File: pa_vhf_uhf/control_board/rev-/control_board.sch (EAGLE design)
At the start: 0 parts

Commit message: minor updates to control board.
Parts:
- added ADC1: ADS1115, vtgs:ADS1115
- added J1: USB_B_PTH, SparkFun-Connectors:USB_B_PTH
- added U$1: SPX3819M5_5V, kj4qlp:V_REG_SPX3819-SOT23-5
- added U$2: ATMEGA32U4-AU, adafruit:ATMEGA32U4-AU
- added U$3: DECOTEC_102040-002B, vtgs:DECOTEC_102040-002B
- added X1: (no value), SparkFun-Retired:DB25_MALED

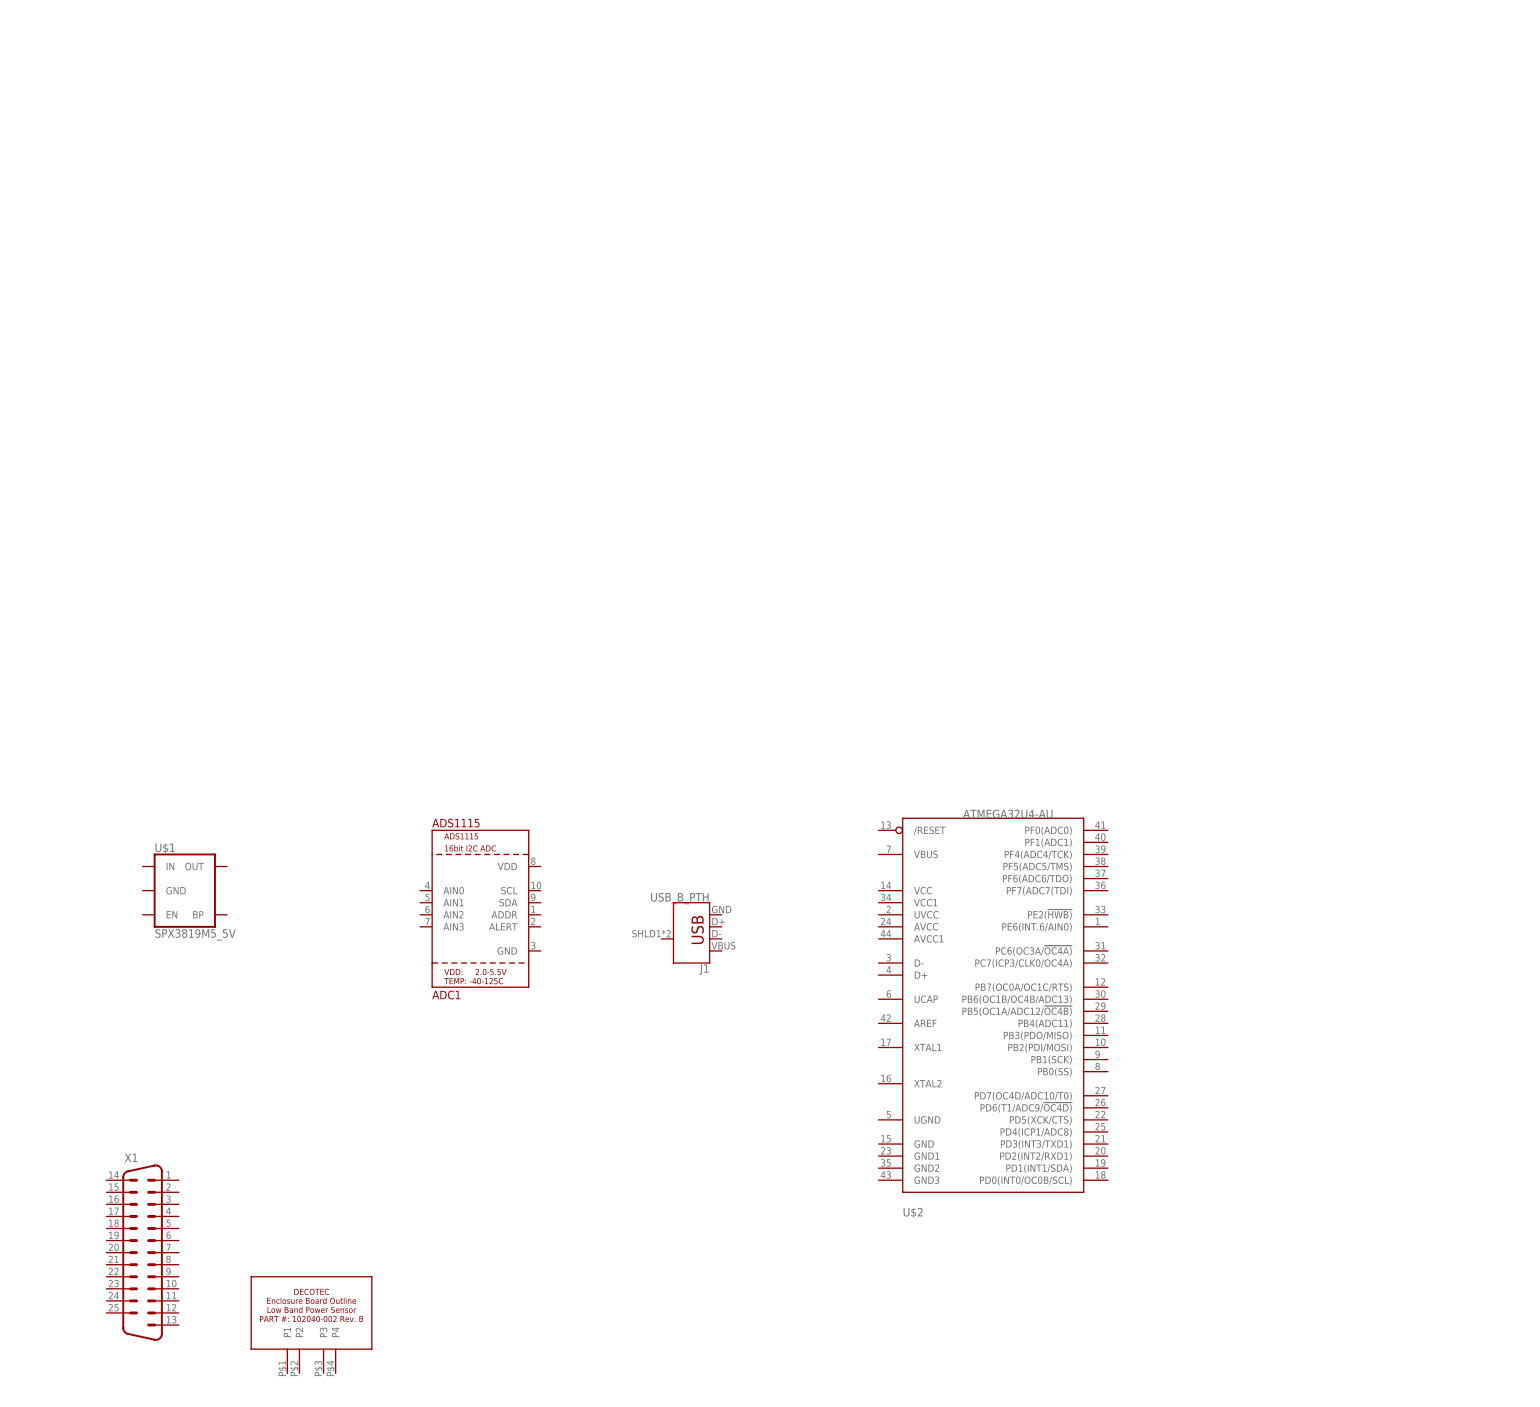
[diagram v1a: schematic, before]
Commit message: lots of updates, almost done, a bit more tweaking/refining of the layout.  need to double check optocoupler current levels/resistors.
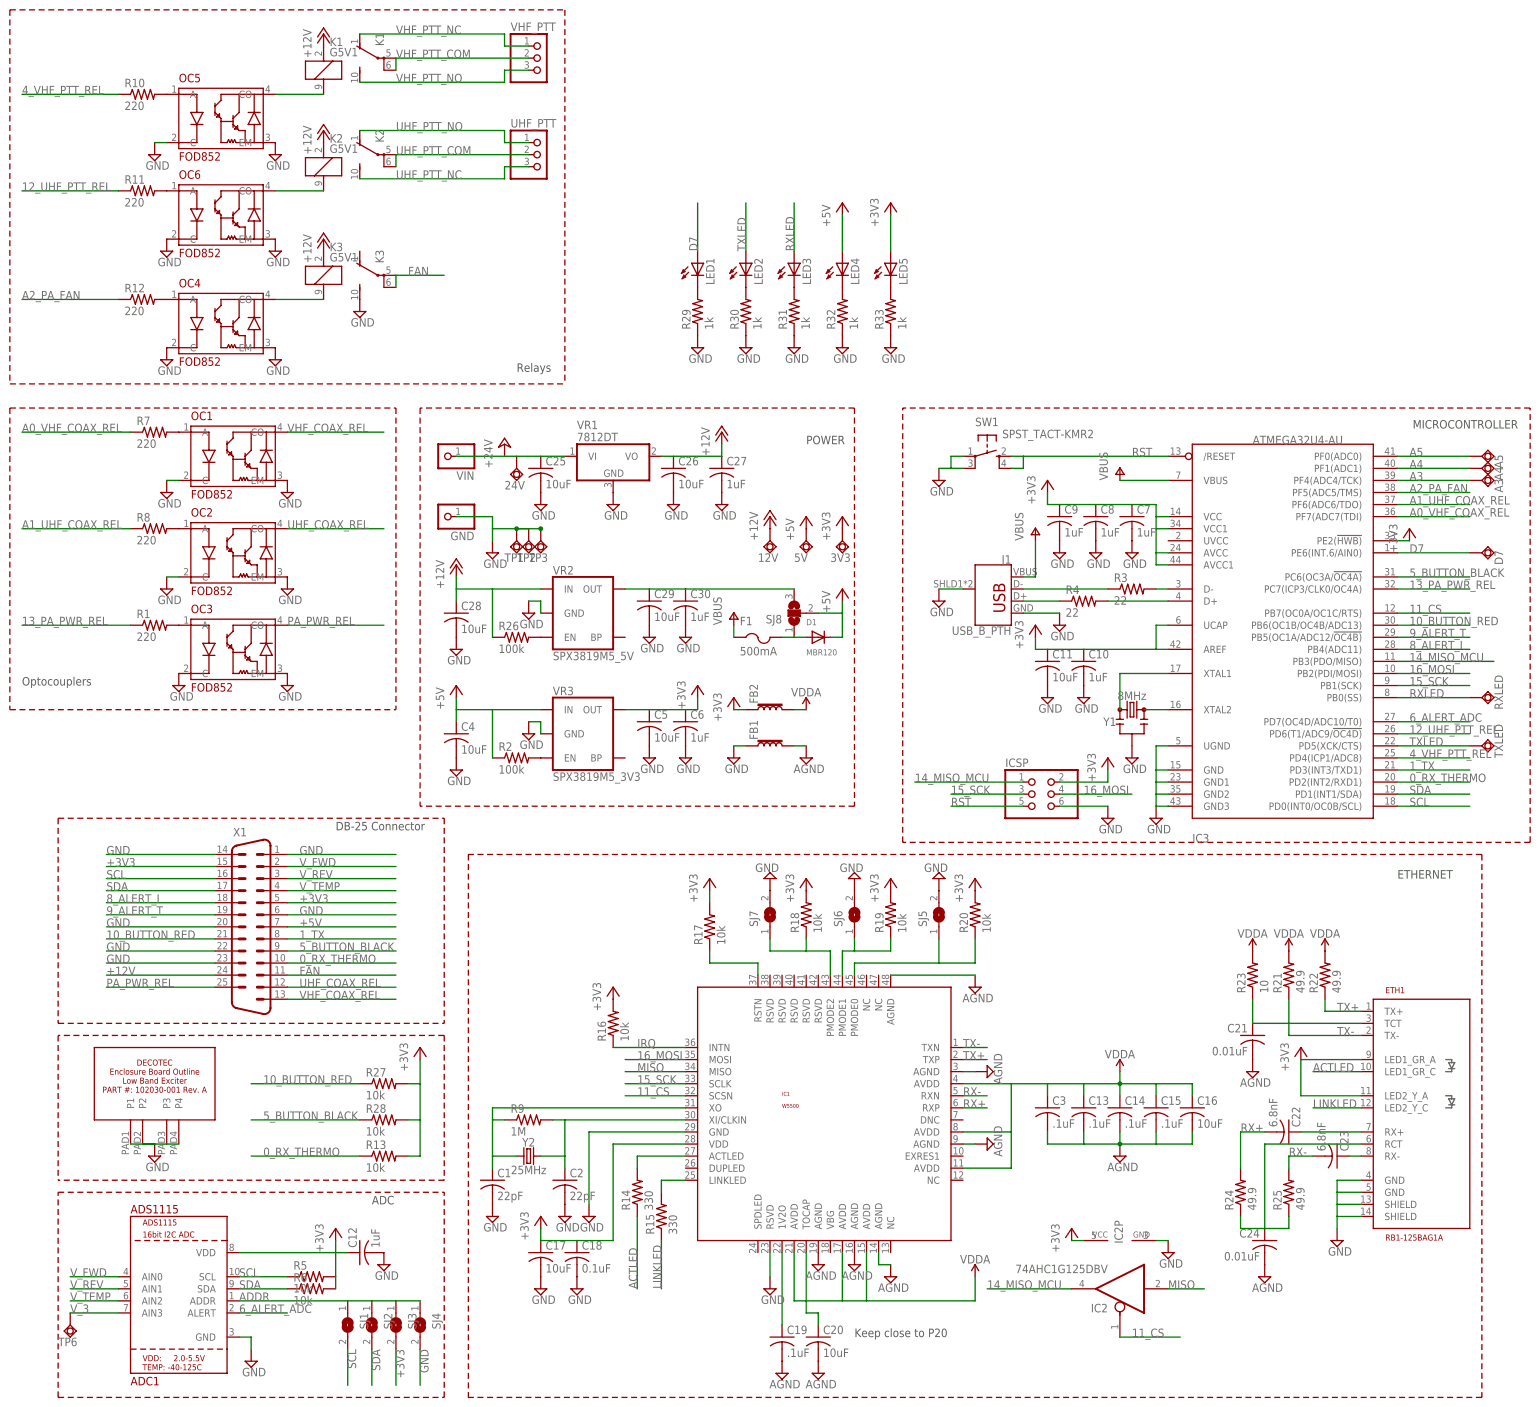
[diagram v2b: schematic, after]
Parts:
- removed U$1: SPX3819M5_5V, kj4qlp:V_REG_SPX3819-SOT23-5
- removed U$2: ATMEGA32U4-AU, adafruit:ATMEGA32U4-AU
- added 12V, 24V, 3V3, 5V, A3, A4, A5, D7, RXLED, TP1, TP2, TP3, TP6, TXLED: TPSQTP20SQ, testpad:TPSQTP20SQ
- added C1, C2: 22pF, rcl:C-USC0805K
- added C10, C12, C27, C30, C6, C7, C8, C9: 1uF, rcl:C-USC0805K
- added C11, C16, C17, C20, C25, C26, C28, C29, C4, C5: 10uF, rcl:C-USC0805K
- added C13, C14, C15, C19, C3: .1uF, rcl:C-USC0805K
- added C18: 0.1uF, rcl:C-USC0805K
- added C21, C24: 0.01uF, rcl:C-USC0805K
- added C22, C23: 6.8nF, rcl:C-USC0805K
- added D1: MBR120, adafruit:DIODESOD-123
- added ETH1: RB1-125BAG1A, vtgs:RB1-125BAG1A
- added F1: 500mA, adafruit:PTCFUSE-1206
- added FB1, FB2: FERRITE_BEAD, vtgs:FERRITE_BEAD
- added GND, VIN: (no value), pinhead:PINHD-1X1
- added IC1: W5500, vtgs:W5500
- added IC2: 74AHC1G125DBV, 74xx-little-us:74AHC1G125DBV
- added IC3: ATMEGA32U4-AU, adafruit:ATMEGA32U4-AU
- added ICSP: (no value), pinhead:PINHD-2X3
- added K1, K2, K3: G5V1, relay:G5V1
- added LED1, LED2, LED3, LED4, LED5: (no value), adafruit:LEDCHIPLED_0805
- added OC1, OC2, OC3, OC4, OC5, OC6: FOD852, vtgs:FOD852
- added R1, R10, R11, R12, R7, R8: 220, rcl:R-US_R0805
- added R13, R16, R17, R18, R19, R20, R27, R28, R5, R6: 10k, rcl:R-US_R0805
- added R14, R15: 330, rcl:R-US_R0805
- added R2, R26: 100k, rcl:R-US_R0805
- added R21, R22, R24, R25: 49.9, rcl:R-US_R0805
- added R23: 10, rcl:R-US_R0805
- added R29, R30, R31, R32, R33: 1k, rcl:R-US_R0805
- added R3, R4: 22, rcl:R-US_R0805
- added R9: 1M, rcl:R-US_R0805
- added SJ1, SJ2, SJ3, SJ4, SJ5, SJ6, SJ7: (no value), jumper:SJ
- added SJ8: (no value), jumper:SJ2W
- added SW1: SPST_TACT-KMR2, adafruit:SPST_TACT-KMR2
- added UHF_PTT, VHF_PTT: (no value), pinhead:PINHD-1X3
- added VR1: 7812DT, adafruit:7812DT
- added VR2: SPX3819M5_5V, kj4qlp:V_REG_SPX3819-SOT23-5
- added VR3: SPX3819M5_3V3, kj4qlp:V_REG_SPX3819-SOT23-5
- added Y1: 8MHz, SparkFun-Clocks:RESONATOR-8MHZSMD_3.2X1.3
- added Y2: 25MHz, SparkFun-Clocks:CRYSTALSMD-3.2X2.5
- U$3: value DECOTEC_102040-002B -> DECOTEC_102030-001AV3; device vtgs:DECOTEC_102040-002B -> vtgs:DECOTEC_102030-001AV3
- X1: device SparkFun-Retired:DB25_MALED -> SparkFun-Retired:DB25_MALEVB
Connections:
- new net +12V: 12V.TP, C26.1, C27.1, C28.1, K11.1, K21.1, K31.1, R26.1, VR1.VO, VR2.IN, X1.24
- new net +24V: 24V.TP, C25.1, VIN.1, VR1.VI
- new net +3V3: 3V3.TP, ADC1.VDD, C10.1, C11.1, C12.1, C17.1, C18.1, C5.1, C6.1, C7.1, C8.1, C9.1, ETH1.LED1_GR_A, ETH1.LED2_Y_A, FB2.1, IC1.VDD, IC2P.VCC, IC3.AREF, IC3.AVCC, IC3.AVCC1, IC3.PE2(!HWB), IC3.UCAP, IC3.VCC, IC3.VCC1, ICSP.2, LED5.A, R13.2, R16.2, R17.2, R18.2, R19.2, R20.2, R27.2, R28.2, R5.2, R6.2, SJ3.2, VR3.OUT, X1.15, X1.5
- new net +5V: 5V.TP, C4.1, D1.C, LED4.A, R2.1, SJ8.2, VR3.IN, X1.7
- new net 0_RX_THERMO: IC3.PD2(INT2/RXD1), R13.1, X1.10
- new net 10_BUTTON_RED: IC3.PB6(OC1B/OC4B/ADC13), R27.1, X1.21
- new net 11_CS: IC1.SCSN, IC2A.OE, IC3.PB7(OC0A/OC1C/RTS)
- new net 12_UHF_PTT_REL: IC3.PD6(T1/ADC9/!OC4D), R11.1
- new net 13_PA_PWR_REL: IC3.PC7(ICP3/CLK0/OC4A), R1.1
- new net 14_MISO_MCU: IC2A.O, IC3.PB3(PDO/MISO), ICSP.1
- new net 15_SCK: IC1.SCLK, IC3.PB1(SCK), ICSP.3
- new net 16_MOSI: IC1.MOSI, IC3.PB2(PDI/MOSI), ICSP.4
- new net 1_TX: IC3.PD3(INT3/TXD1), X1.8
- new net 4_VHF_PTT_REL: IC3.PD4(ICP1/ADC8), R10.1
- new net 5_BUTTON_BLACK: IC3.PC6(OC3A/!OC4A), R28.1, X1.9
- new net 6_ALERT_ADC: ADC1.ALERT, IC3.PD7(OC4D/ADC10/T0)
- new net 8_ALERT_I: IC3.PB4(ADC11), X1.18
- new net 9_ALERT_T: IC3.PB5(OC1A/ADC12/!OC4B), X1.19
- new net A0_VHF_COAX_REL: IC3.PF7(ADC7(TDI), R7.1
- new net A1_UHF_COAX_REL: IC3.PF6(ADC6/TDO), R8.1
- new net A2_PA_FAN: IC3.PF5(ADC5/TMS), R12.1
- new net A3: A3.TP, IC3.PF4(ADC4/TCK)
- new net A4: A4.TP, IC3.PF1(ADC1)
- new net A5: A5.TP, IC3.PF0(ADC0)
- new net ACTLED: ETH1.LED1_GR_C, R14.1
- new net ADDR: ADC1.ADDR, SJ1.1, SJ2.1, SJ3.1, SJ4.1
- new net AGND: C13.2, C14.2, C15.2, C16.2, C19.2, C20.2, C21.2, C24.2, C3.2, FB1.2, IC1.AGND@14, IC1.AGND@16, IC1.AGND@19, IC1.AGND@3, IC1.AGND@48, IC1.AGND@9
- new net D7: D7.TP, IC3.PE6(INT.6/AIN0), LED1.A
- new net FAN: K32.P, K32.P@1, X1.11
- new net GND: ADC1.GND, C1.2, C10.2, C11.2, C12.2, C17.2, C18.2, C2.2, C25.2, C26.2, C27.2, C28.2, C29.2, C30.2, C4.2, C5.2, C6.2, C7.2, C8.2, C9.2, ETH1.GND@1, ETH1.GND@2, ETH1.SHIELD@1, ETH1.SHIELD@2, FB1.1, GND.1, IC1.GND, IC1.RSVD, IC2P.GND, IC3.GND, IC3.GND1, IC3.GND2, IC3.GND3, IC3.UGND, ICSP.6, J1.GND, J1.SHIELD, K32.S, OC1.C, OC1.EM, OC2.C, OC2.EM, OC3.C, OC3.EM, OC4.C, OC4.EM, OC5.C, OC5.EM, OC6.C, OC6.EM, R29.1, R30.1, R31.1, R32.1, R33.1, SJ4.2, SJ5.2, SJ6.2, SJ7.2, SW1.P, SW1.P1, TP1.TP, TP2.TP, TP3.TP, U$3.P1, U$3.P2, U$3.P3, U$3.P4, VR1.GND, VR2.GND, VR3.GND, X1.1, X1.14, X1.20, X1.22, X1.23, X1.6, Y1.2
- new net IRQ: IC1.INTN, R16.1
- new net LINKLED: ETH1.LED2_Y_C, R15.1
- new net MISO: IC1.MISO, IC2A.I
- new net N$1: OC3.A, R1.2
- new net N$10: IC3.D+, R4.2
- new net N$11: J1.D+, R4.1
- new net N$12: OC1.A, R7.2
- new net N$13: OC2.A, R8.2
- new net N$14: IC1.RSTN, R17.1
- new net N$15: OC5.A, R10.2
- new net N$16: LED1.C, R29.2
- new net N$17: LED2.C, R30.2
- new net N$18: LED4.C, R32.2
- new net N$19: LED5.C, R33.2
- new net N$2: K31.2, OC4.CO
- new net N$20: OC6.A, R11.2
- new net N$21: OC4.A, R12.2
- new net N$22: K11.2, OC5.CO
- new net N$23: K21.2, OC6.CO
- new net N$24: LED3.C, R31.2
- new net N$29: IC1.ACTLED, R14.2
- new net N$3: R2.2, VR3.EN
- new net N$30: IC1.LINKLED, R15.2
- new net N$31: C29.1, C30.1, SJ8.3, VR2.OUT
- new net N$33: C20.1, IC1.TOCAP
- new net N$34: C19.1, IC1.1V2O
- new net N$35: C23.1, ETH1.RX-
- new net N$36: C22.1, ETH1.RX+
- new net N$37: C24.1, ETH1.RCT, R24.1, R25.1
- new net N$38: R26.2, VR2.EN
- new net N$39: D1.A, F1.2, SJ8.1
- new net N$4: IC3.XTAL1, Y1.1
- new net N$5: IC3.XTAL2, Y1.3
- new net N$6: C1.1, IC1.XO, R9.1, Y2.1
- new net N$7: C2.1, IC1.XI/CLKIN, R9.2, Y2.2
- new net N$8: J1.D-, R3.1
- new net N$9: IC3.D-, R3.2
- new net PA_PWR_REL: OC3.CO, X1.25
- new net PMODE0: IC1.PMODE0, R20.1, SJ5.1
- new net PMODE1: IC1.PMODE1, R19.1, SJ6.1
- new net PMODE2: IC1.PMODE2, R18.1, SJ7.1
- new net RST: IC3./RESET, ICSP.5, SW1.S, SW1.S1
- new net RX+: C22.2, IC1.RXP, R24.2
- new net RX-: C23.2, IC1.RXN, R25.2
- new net RXLED: IC3.PB0(SS), LED3.A, RXLED.TP
- new net SCL: ADC1.SCL, IC3.PD0(INT0/OC0B/SCL), R5.1, SJ1.2, X1.16
- new net SDA: ADC1.SDA, IC3.PD1(INT1/SDA), R6.1, SJ2.2, X1.17
- new net TCT: C21.1, ETH1.TCT, R23.1
- new net TX+: ETH1.TX+, IC1.TXP, R22.1
- new net TX-: ETH1.TX-, IC1.TXN, R21.1
- new net TXLED: IC3.PD5(XCK/CTS), LED2.A, TXLED.TP
- new net UHF_COAX_REL: OC2.CO, X1.12
- new net UHF_PTT_COM: K22.P, K22.P@1, UHF_PTT.2
- new net UHF_PTT_NC: K22.S, UHF_PTT.3
- new net UHF_PTT_NO: K22.O, UHF_PTT.1
- new net VBUS: F1.1, IC3.VBUS, J1.VBUS
- new net VDDA: C13.1, C14.1, C15.1, C16.1, C3.1, FB2.2, IC1.AVDD@11, IC1.AVDD@15, IC1.AVDD@17, IC1.AVDD@21, IC1.AVDD@4, IC1.AVDD@8, R21.2, R22.2, R23.2
- new net VHF_COAX_REL: OC1.CO, X1.13
- new net VHF_PTT_COM: K12.P, K12.P@1, VHF_PTT.2
- new net VHF_PTT_NC: K12.O, VHF_PTT.1
- new net VHF_PTT_NO: K12.S, VHF_PTT.3
- new net V_3: ADC1.AIN3, TP6.TP
- new net V_FWD: ADC1.AIN0, X1.2
- new net V_REV: ADC1.AIN1, X1.3
- new net V_TEMP: ADC1.AIN2, X1.4
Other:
- note added: "ADC"
- note added: "DB-25 Connector"
- note added: "ETHERNET"
- note added: "Keep close to P20"
- note added: "MICROCONTROLLER"
- note added: "Optocouplers"
- note added: "POWER"
- note added: "Relays"
- moved on the sheet: ADC1, J1, X1

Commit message: Final Commit for Rev-.  This version submitted to osh park for fab.
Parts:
- removed C30: 1uF, rcl:C-USC0805K
- removed GND, VIN: (no value), pinhead:PINHD-1X1
- removed TP2, TP3, TP6: TPSQTP20SQ, testpad:TPSQTP20SQ
- removed VR1: 7812DT, adafruit:7812DT
- added CASE_TEMP: (no value), pinhead:PINHD-1X3
- added DIS: (no value), pinhead:PINHD-1X2
- added KA278R12C: (no value), pinhead:PINHD-1X6
- added R34, R35, R36, R37, R38, R39: 10, rcl:R-US_R0805
- added R40: 10k, rcl:R-US_R0805
- A3, A4, A5, D7, IC3, ICSP, J1, RXLED, TXLED: SPICEPREFIX (none) -> X
- C1, C2: value 22pF -> 12pF
- C18: value 0.1uF -> .1uF
- C25: value 10uF -> 33uF; device rcl:C-USC0805K -> rcl:CPOL-USC
- C26: value 10uF -> 100uF; device rcl:C-USC0805K -> rcl:CPOL-USD
- C27: value 1uF -> 10uF
- C29: value 10uF -> 1uF
- SW1: SPICEPREFIX (none) -> S
- Y1: SPICEPREFIX (none) -> J
- Y2: value 25MHz -> 25MHz, 10pF
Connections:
- removed net V_3: ADC1.AIN3, TP6.TP
- new net N$25: OC5.EM, R34.1
- new net N$26: OC6.EM, R35.1
- new net N$27: OC4.EM, R36.1
- new net N$28: OC1.EM, R37.1
- new net N$32: OC2.EM, R38.1
- new net N$40: OC3.EM, R39.1
- new net N$41: DIS.1, KA278R12C.5, R40.1
- new net V_CASE: ADC1.AIN3, CASE_TEMP.3
- net +12V: now also C26.+, KA278R12C.3; no longer C26.1, C28.1, VR1.VO
- net +24V: now also C25.+, KA278R12C.1, KA278R12C.2, R40.2; no longer C25.1, VIN.1, VR1.VI
- net +3V3: now also CASE_TEMP.2
- net GND: now also C25.-, C26.-, CASE_TEMP.1, DIS.2, KA278R12C.4, KA278R12C.6, R34.2, R35.2, R36.2, R37.2, R38.2, R39.2; no longer C25.2, C26.2, C30.2, GND.1, OC1.EM, OC2.EM, OC3.EM, OC4.EM, OC5.EM, OC6.EM, TP2.TP, TP3.TP, VR1.GND
- net N$31: now also C28.1; no longer C30.1
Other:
- moved on the sheet: 12V, 24V, 3V3, 5V, A3, A4, A5, ADC1, C1, C10, C11, C12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
